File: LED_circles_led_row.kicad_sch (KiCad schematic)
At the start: 18 parts

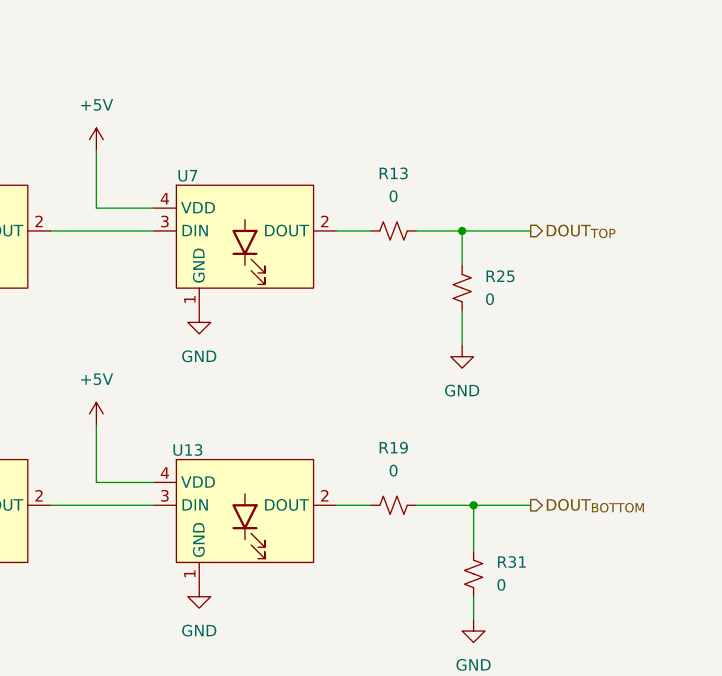
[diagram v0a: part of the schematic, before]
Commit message: Initial layout of top layer
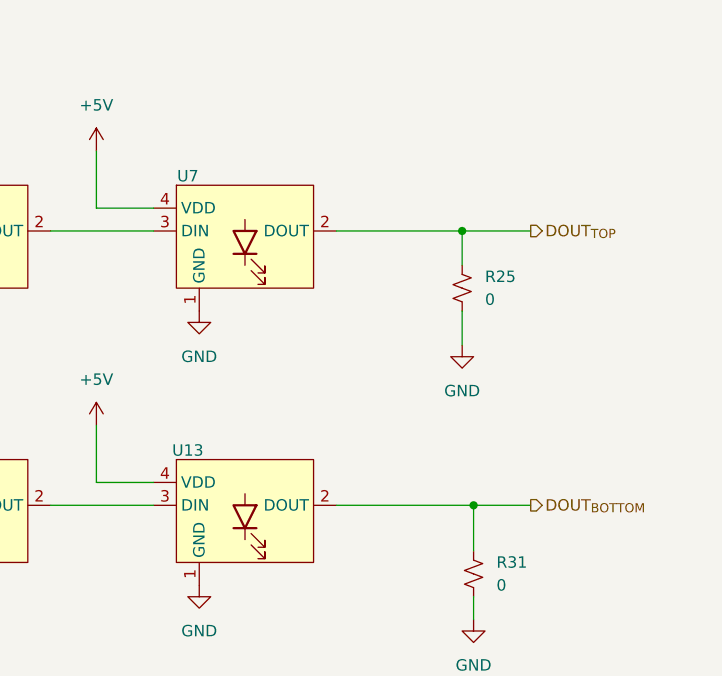
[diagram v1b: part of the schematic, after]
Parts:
- removed R13, R19: 0, Resistor_SMD:R_0805_2012Metric, symbol Device:R_Small_US
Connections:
- net DOUT_{BOTTOM}: now also U13.2 (DOUT)
- net DOUT_{TOP}: now also U7.2 (DOUT)
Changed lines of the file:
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@@
 	(wire
 		(pts
-			(xy 308.61 105.41) (xy 312.42 105.41)
+			(xy 308.61 105.41) (xy 322.58 105.41)
 		)
 		(stroke
@@
 	(wire
 		(pts
-			(xy 317.5 105.41) (xy 322.58 105.41)
+			(xy 218.44 105.41) (xy 228.6 105.41)
 		)
 		(stroke
@@
 	(wire
 		(pts
-			(xy 218.44 105.41) (xy 228.6 105.41)
+			(xy 250.19 133.35) (xy 250.19 127)
 		)
 		(stroke
@@
 	(wire
 		(pts
-			(xy 317.5 135.89) (xy 323.85 135.89)
+			(xy 198.12 102.87) (xy 191.77 102.87)
 		)
 		(stroke
@@
 	(wire
 		(pts
-			(xy 250.19 133.35) (xy 250.19 127)
+			(xy 191.77 102.87) (xy 191.77 96.52)
 		)
 		(stroke
@@
 	(wire
 		(pts
-			(xy 198.12 102.87) (xy 191.77 102.87)
+			(xy 222.25 133.35) (xy 222.25 127)
 		)
 		(stroke
@@
 	(wire
 		(pts
-			(xy 191.77 102.87) (xy 191.77 96.52)
+			(xy 118.11 105.41) (xy 135.89 105.41)
 		)
 		(stroke
@@
 	(wire
 		(pts
-			(xy 222.25 133.35) (xy 222.25 127)
+			(xy 276.86 135.89) (xy 288.29 135.89)
 		)
 		(stroke
@@
 	(wire
 		(pts
-			(xy 118.11 105.41) (xy 135.89 105.41)
+			(xy 156.21 105.41) (xy 167.64 105.41)
 		)
 		(stroke
@@
 	(wire
 		(pts
-			(xy 276.86 135.89) (xy 288.29 135.89)
+			(xy 119.38 135.89) (xy 135.89 135.89)
 		)
 		(stroke
@@
 	(wire
 		(pts
-			(xy 156.21 105.41) (xy 167.64 105.41)
+			(xy 248.92 105.41) (xy 256.54 105.41)
 		)
 		(stroke
@@
 	(wire
 		(pts
-			(xy 119.38 135.89) (xy 135.89 135.89)
+			(xy 161.29 102.87) (xy 161.29 96.52)
 		)
 		(stroke
@@
 	(wire
 		(pts
-			(xy 248.92 105.41) (xy 256.54 105.41)
+			(xy 109.22 105.41) (xy 113.03 105.41)
 		)
 		(stroke
@@
 	(wire
 		(pts
-			(xy 161.29 102.87) (xy 161.29 96.52)
-		)
-		(stroke
-			(width 0)
-			(type default)
-		)
-	)
-	(wire
-		(pts
-			(xy 109.22 105.41) (xy 113.03 105.41)
-		)
-		(stroke
-			(width 0)
-			(type default)
-		)
-	)
-	(wire
-		(pts
-			(xy 308.61 135.89) (xy 312.42 135.89)
+			(xy 308.61 135.89) (xy 323.85 135.89)
 		)
 		(stroke
@@
 	)
 	(symbol
-		(lib_id "Device:R_Small_US")
-		(at 314.96 135.89 90)
-		(unit 1)
-		(exclude_from_sim no)
-		(in_bom yes)
-		(on_board yes)
-		(dnp no)
-		(fields_autoplaced yes)
-		(property "Reference" "R19"
-			(at 314.96 129.54 90)
-			(effects
-				(font
-					(size 1.27 1.27)
-				)
-			)
-		)
-		(property "Value" "0"
-			(at 314.96 132.08 90)
-			(effects
-				(font
-					(size 1.27 1.27)
-				)
-			)
-		)
-		(property "Footprint" "Resistor_SMD:R_0805_2012Metric"
-			(at 314.96 135.89 0)
-			(effects
-				(font
-					(size 1.27 1.27)
-				)
-				(hide yes)
-			)
-		)
-		(property "Datasheet" "~"
-			(at 314.96 135.89 0)
-			(effects
-				(font
-					(size 1.27 1.27)
-				)
-				(hide yes)
-			)
-		)
-		(property "Description" "Resistor, small US symbol"
-			(at 314.96 135.89 0)
-			(effects
-				(font
-					(size 1.27 1.27)
-				)
-				(hide yes)
-			)
-		)
-		(pin "1"
-		)
-		(pin "2"
-		)
-		(instances
-			(project "LED_circles"
-				(path "/fee5cc62-df5b-4e25-a1c9-d9673ac3b8e2/44e8ba91-3a10-488a-90ac-cab22a61c6c4"
-					(reference "R22")
-					(unit 1)
-				)
-				(path "/fee5cc62-df5b-4e25-a1c9-d9673ac3b8e2/72301e72-b154-4705-8921-79efe84e134a"
-					(reference "R21")
-					(unit 1)
-				)
-				(path "/fee5cc62-df5b-4e25-a1c9-d9673ac3b8e2/72c08671-0611-4d20-b947-89e2fde69567"
-					(reference "R19")
-					(unit 1)
-				)
-				(path "/fee5cc62-df5b-4e25-a1c9-d9673ac3b8e2/9310fa55-8873-4e7f-96c0-a68569c657d5"
-					(reference "R23")
-					(unit 1)
-				)
-				(path "/fee5cc62-df5b-4e25-a1c9-d9673ac3b8e2/9b430a50-2d65-43e0-95df-92b936891a2b"
-					(reference "R20")
-					(unit 1)
-				)
-				(path "/fee5cc62-df5b-4e25-a1c9-d9673ac3b8e2/ef117ddb-61a6-4981-a672-4813b9746f59"
-					(reference "R24")
-					(unit 1)
-				)
-			)
-		)
-	)
-	(symbol
 		(lib_id "LED_circles_library:IN-PI55TATPRPGPB")
 		(at 298.45 137.16 0)
@@
 					(unit 1)
 				)
-			)
-		)
-	)
-	(symbol
-		(lib_id "Device:R_Small_US")
-		(at 314.96 105.41 90)
-		(unit 1)
-		(exclude_from_sim no)
-		(in_bom yes)
-		(on_board yes)
-		(dnp no)
-		(fields_autoplaced yes)
-		(property "Reference" "R13"
-			(at 314.96 99.06 90)
-			(effects
-				(font
-					(size 1.27 1.27)
-				)
-			)
-		)
-		(property "Value" "0"
-			(at 314.96 101.6 90)
-			(effects
-				(font
-					(size 1.27 1.27)
-				)
-			)
-		)
-		(property "Footprint" "Resistor_SMD:R_0805_2012Metric"
-			(at 314.96 105.41 0)
-			(effects
-				(font
-					(size 1.27 1.27)
-				)
-				(hide yes)
-			)
-		)
-		(property "Datasheet" "~"
-			(at 314.96 105.41 0)
-			(effects
-				(font
-					(size 1.27 1.27)
-				)
-				(hide yes)
-			)
-		)
-		(property "Description" "Resistor, small US symbol"
-			(at 314.96 105.41 0)
-			(effects
-				(font
-					(size 1.27 1.27)
-				)
-				(hide yes)
-			)
-		)
-		(pin "1"
-		)
-		(pin "2"
-		)
-		(instances
-			(project "LED_circles"
-				(path "/fee5cc62-df5b-4e25-a1c9-d9673ac3b8e2/44e8ba91-3a10-488a-90ac-cab22a61c6c4"
-					(reference "R16")
-					(unit 1)
-				)
-				(path "/fee5cc62-df5b-4e25-a1c9-d9673ac3b8e2/72301e72-b154-4705-8921-79efe84e134a"
-					(reference "R15")
-					(unit 1)
-				)
-				(path "/fee5cc62-df5b-4e25-a1c9-d9673ac3b8e2/72c08671-0611-4d20-b947-89e2fde69567"
-					(reference "R13")
-					(unit 1)
-				)
-				(path "/fee5cc62-df5b-4e25-a1c9-d9673ac3b8e2/9310fa55-8873-4e7f-96c0-a68569c657d5"
-					(reference "R17")
-					(unit 1)
-				)
-				(path "/fee5cc62-df5b-4e25-a1c9-d9673ac3b8e2/9b430a50-2d65-43e0-95df-92b936891a2b"
-					(reference "R14")
-					(unit 1)
-				)
-				(path "/fee5cc62-df5b-4e25-a1c9-d9673ac3b8e2/ef117ddb-61a6-4981-a672-4813b9746f59"
-					(reference "R18")
-					(unit 1)
-				)

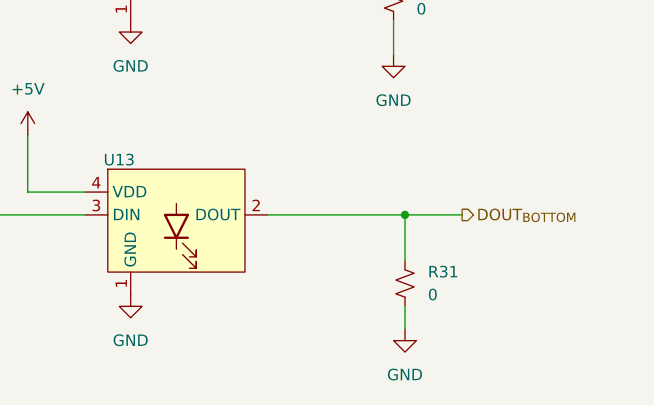
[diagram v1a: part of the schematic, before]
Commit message: Fixed PCB DRC issues.
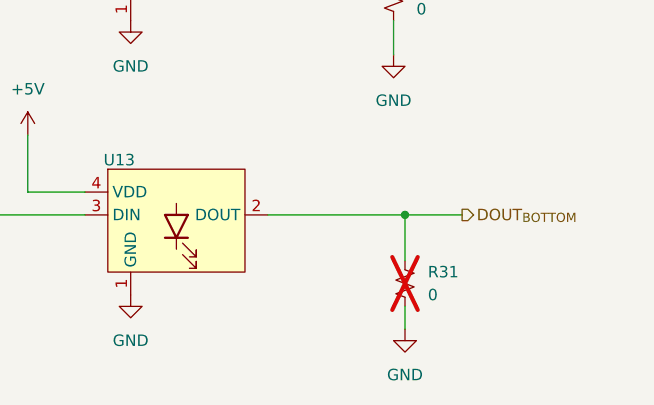
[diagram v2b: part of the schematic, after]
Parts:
- R31: now not fitted
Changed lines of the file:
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@@
 		(in_bom yes)
 		(on_board yes)
-		(dnp no)
+		(dnp yes)
 		(fields_autoplaced yes)
 		(property "Reference" "R31"

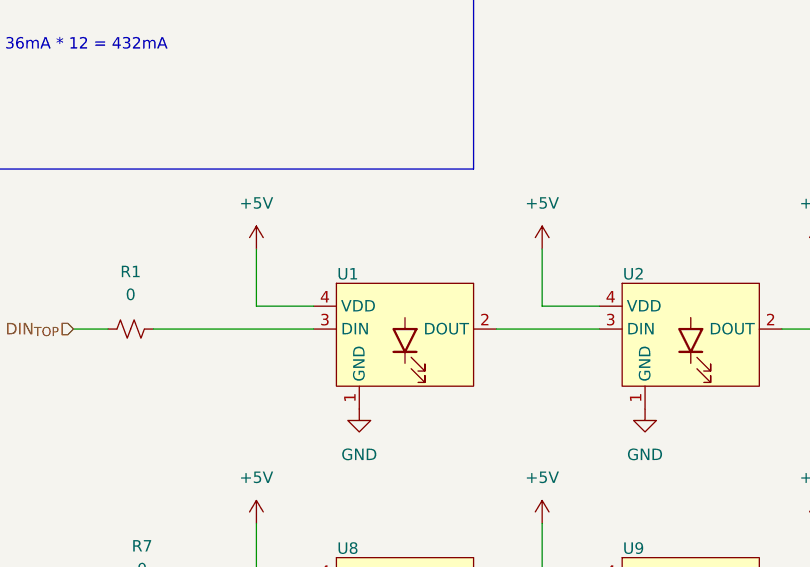
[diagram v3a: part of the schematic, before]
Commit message: Increased track width
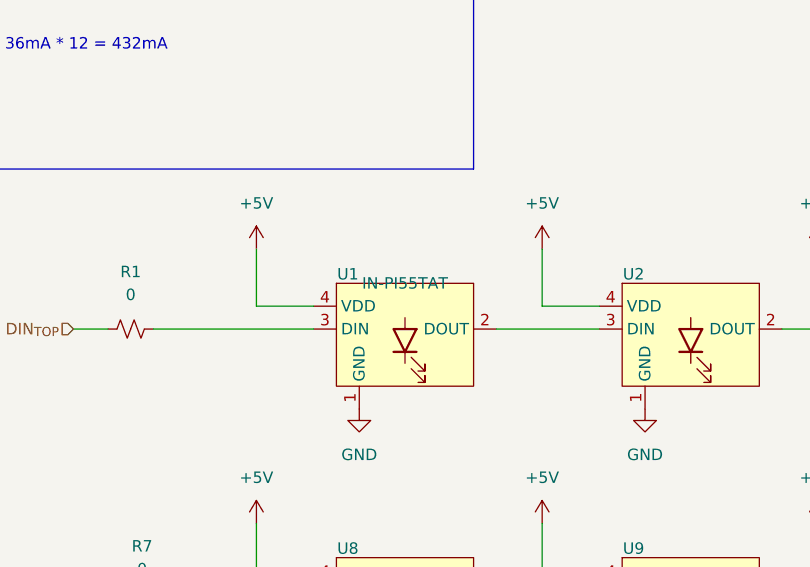
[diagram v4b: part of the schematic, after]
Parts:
- U1: value ~ -> IN-PI55TAT
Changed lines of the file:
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@@
 			)
 		)
-		(property "Value" "~"
+		(property "Value" "IN-PI55TAT"
 			(at 146.05 100.33 0)
 			(effects
